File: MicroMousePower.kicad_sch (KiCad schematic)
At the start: 25 parts, among them J1 USB_C_Receptacle_PowerOnly_6P, J2 Conn_02x16_Odd_Even, T1 TIP31C, U1 INA219AxDCN, U2 MCP73831-3-MC, U3 CH224K, U4 DRV8833PW

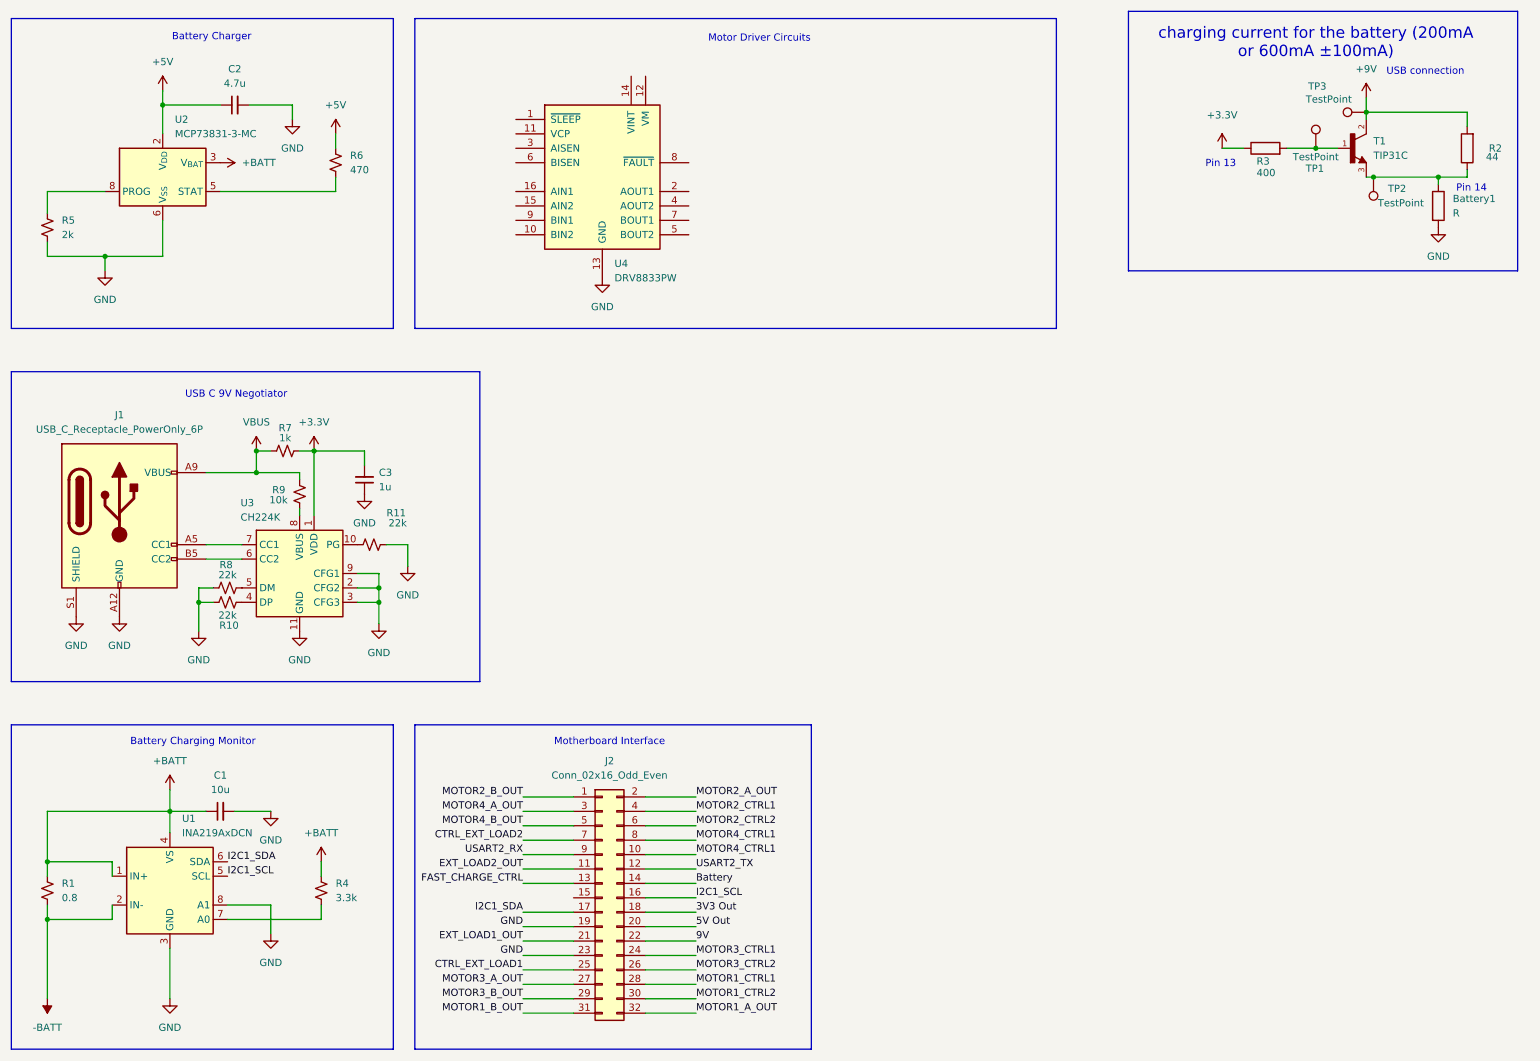
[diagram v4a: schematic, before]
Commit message: connected motor driver circuit
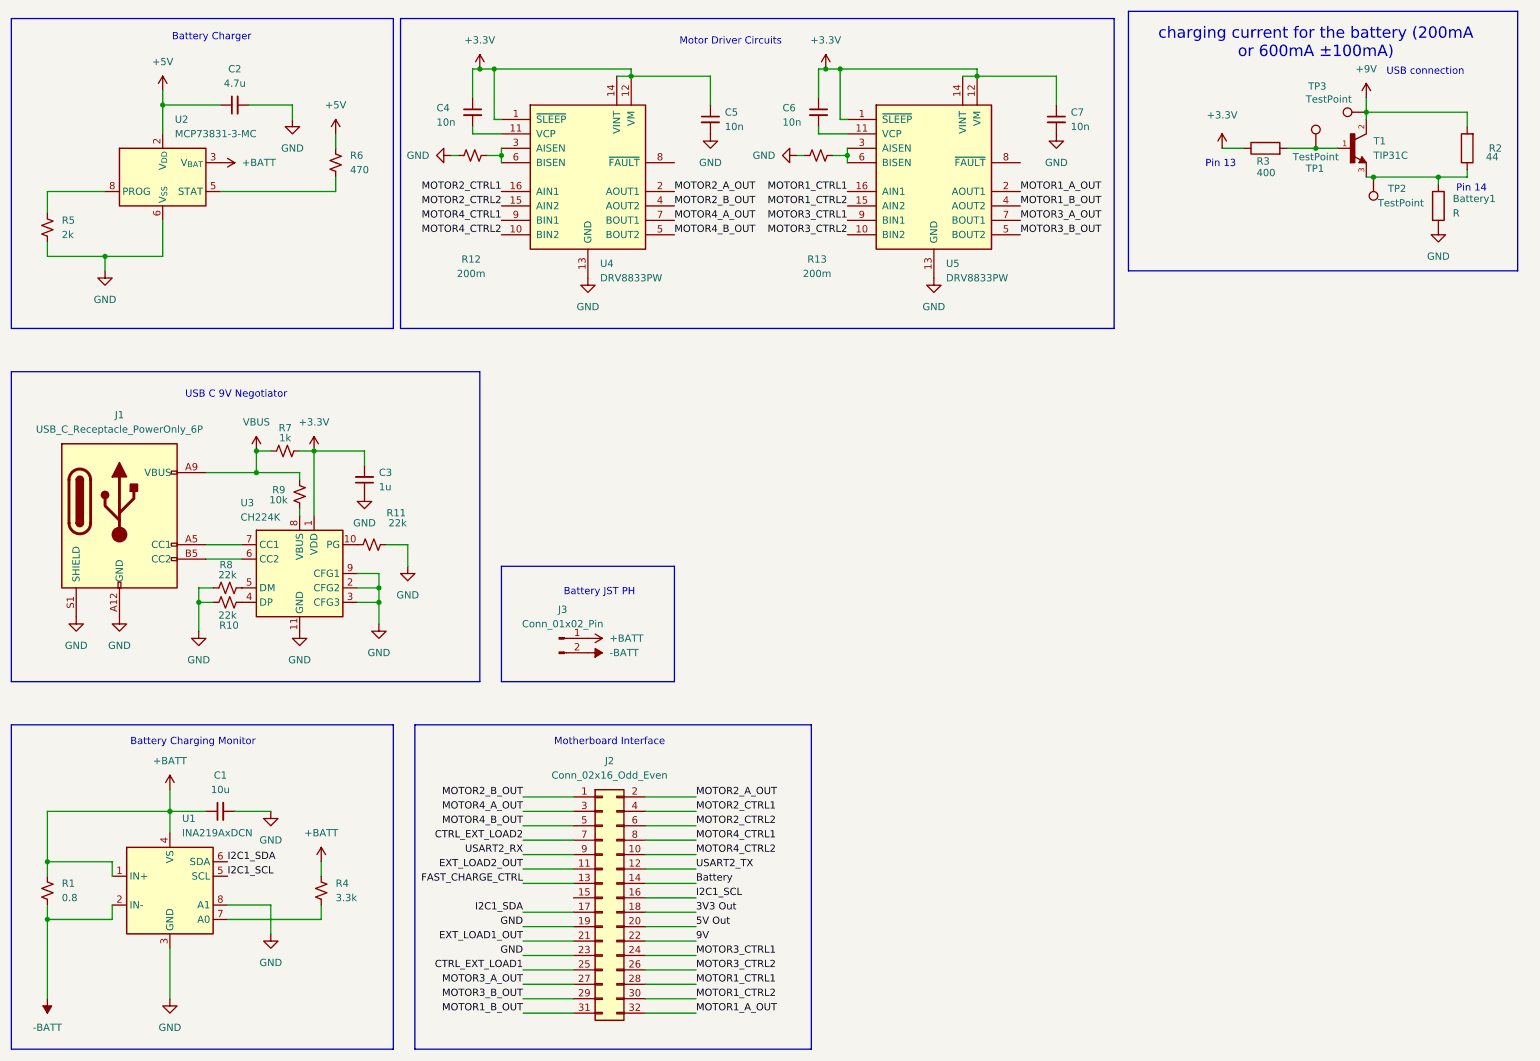
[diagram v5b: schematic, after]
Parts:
- added C4, C5, C6, C7: 10n, symbol Device:C_Small
- added J3: Conn_01x02_Pin, symbol Connector:Conn_01x02_Pin
- added R12, R13: 200m, symbol Device:R_Small_US
- added U5: DRV8833PW, Package_SO:TSSOP-16_4.4x5mm_P0.65mm, symbol Driver_Motor:DRV8833PW
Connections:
- net +3.3V: now also U4.1 (~{SLEEP}), U4.12 (VM), U4.14 (VINT), C4.1, C5.1, C6.1, C7.1, U5.1 (~{SLEEP}), U5.12 (VM), U5.14 (VINT)
- net +BATT: now also J3.1 (Pin_1)
- net -BATT: now also J3.2 (Pin_2)
- net GND: now also C5.2, C7.2, R12.1, R13.1, U5.13 (GND)
- net MOTOR1_A_OUT: now also U5.2 (AOUT1)
- net MOTOR1_B_OUT: now also U5.4 (AOUT2)
- net MOTOR1_CTRL1: now also U5.16 (AIN1)
- net MOTOR1_CTRL2: now also U5.15 (AIN2)
- net MOTOR2_A_OUT: now also U4.2 (AOUT1)
- net MOTOR2_B_OUT: now also U4.4 (AOUT2)
- net MOTOR2_CTRL1: now also U4.16 (AIN1)
- net MOTOR2_CTRL2: now also U4.15 (AIN2)
- net MOTOR3_A_OUT: now also U5.7 (BOUT1)
- net MOTOR3_B_OUT: now also U5.5 (BOUT2)
- net MOTOR3_CTRL1: now also U5.9 (BIN1)
- net MOTOR3_CTRL2: now also U5.10 (BIN2)
- net MOTOR4_A_OUT: now also U4.7 (BOUT1)
- net MOTOR4_B_OUT: now also U4.5 (BOUT2)
- net MOTOR4_CTRL1: now also U4.9 (BIN1); no longer J2.10 (Pin_10)
- net MOTOR4_CTRL2: now reaches U4.10 (BIN2)
- net MOTOR4_CTRL2: now also J2.10 (Pin_10)
- net at U4.11 (VCP): now also C4.2
- net at U4.3 (AISEN): now also U4.6 (BISEN), R12.2
- new net: C6.2, U5.11 (VCP)
- new net: R13.2, U5.3 (AISEN), U5.6 (BISEN)
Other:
- note added: "Battery JST PH"
- moved on the sheet: U4

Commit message: power flag defintions for ERC
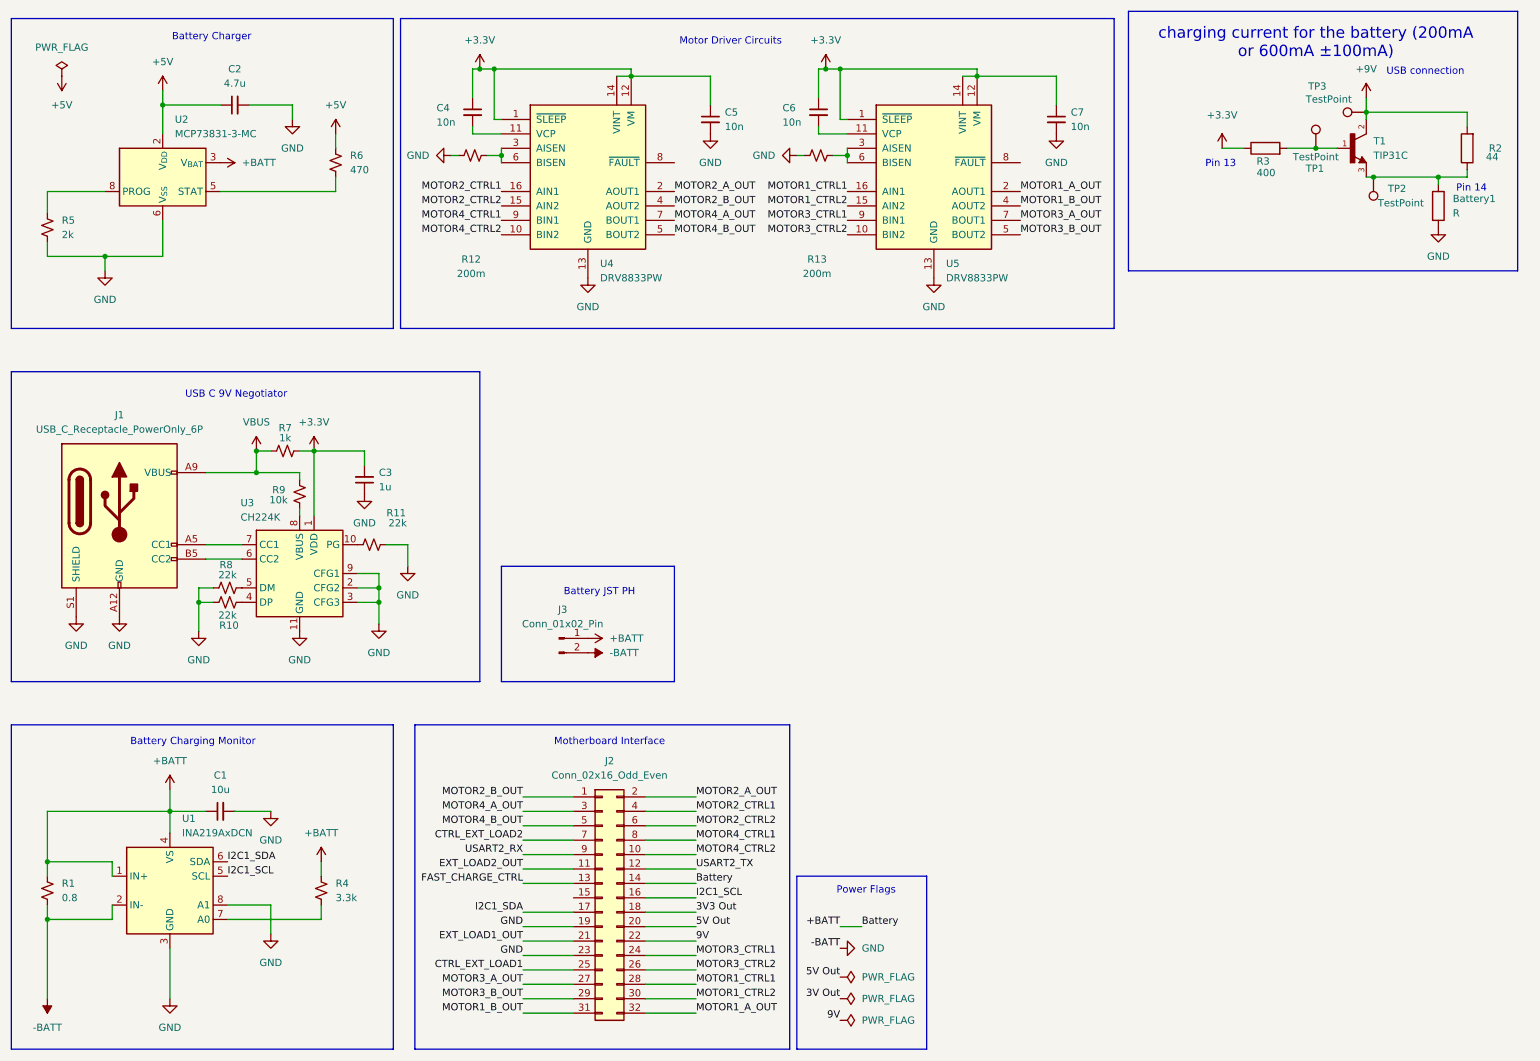
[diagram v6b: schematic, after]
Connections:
- net Battery is gone; now on net +BATT: J2.14 (Pin_14)
- net GND is gone; now on net -BATT: Battery1.2, C1.2, C2.2, C3.1, C5.2, C7.2, J1.A12 (GND), J1.B12 (GND), J1.S1 (SHIELD), J2.19 (Pin_19), J2.23 (Pin_23), R10.2, R11.2, R12.1, R13.1, R5.2, R8.1, U1.3 (GND), U1.8 (A1), U2.6 (V_{SS}), U3.11 (GND), U3.2 (CFG2), U3.3 (CFG3), U3.9 (CFG1), U4.13 (GND), U5.13 (GND)
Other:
- note added: "Power Flags"

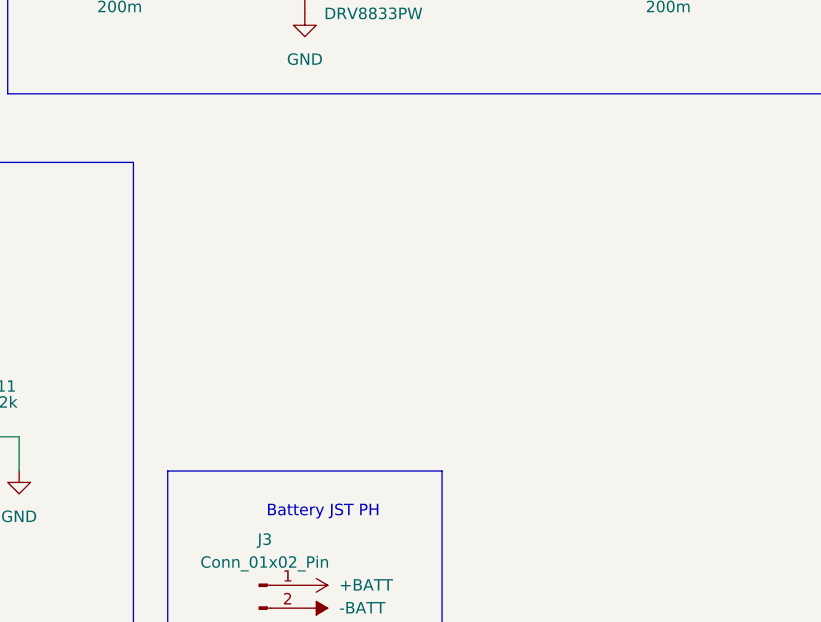
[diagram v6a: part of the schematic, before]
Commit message: template for step down IC
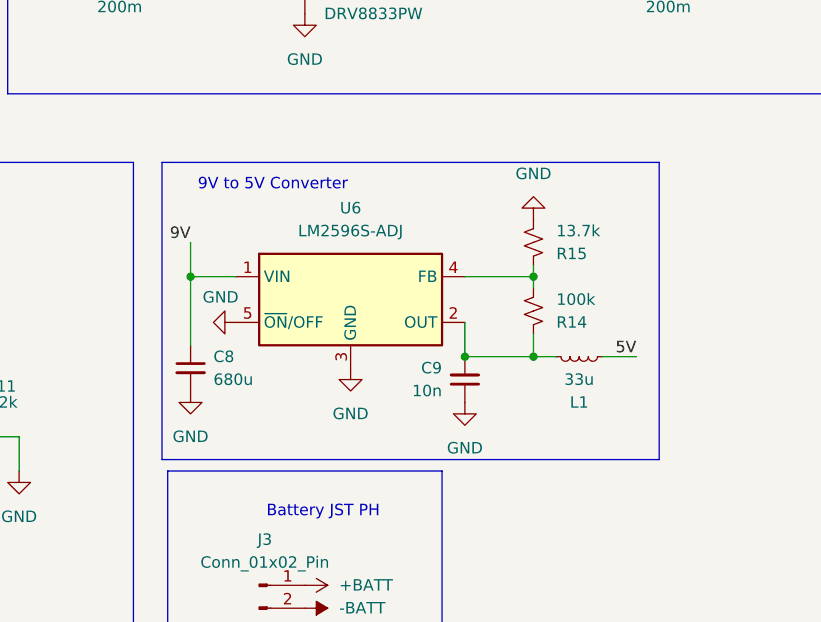
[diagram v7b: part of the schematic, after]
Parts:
- added C8: 680u, symbol Device:C_Small
- added C9: 10n, symbol Device:C_Small
- added L1: 33u, symbol Device:L_Small
- added R14: 100k, symbol Device:R_Small_US
- added R15: 13.7k, symbol Device:R_Small_US
- added U6: LM2596S-ADJ, Package_TO_SOT_SMD:TO-263-5_TabPin3, symbol Regulator_Switching:LM2596S-ADJ
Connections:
- net -BATT: now also C8.2, C9.1, R15.2, U6.3 (GND), U6.5 (~{ON}/OFF)
- net 9V: now also C8.1, U6.1 (VIN)
- new net: C9.2, L1.1, R14.1, U6.2 (OUT)
- new net: R14.2, R15.1, U6.4 (FB)
- new net 5V: L1.2
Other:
- note added: "9V to 5V Converter"

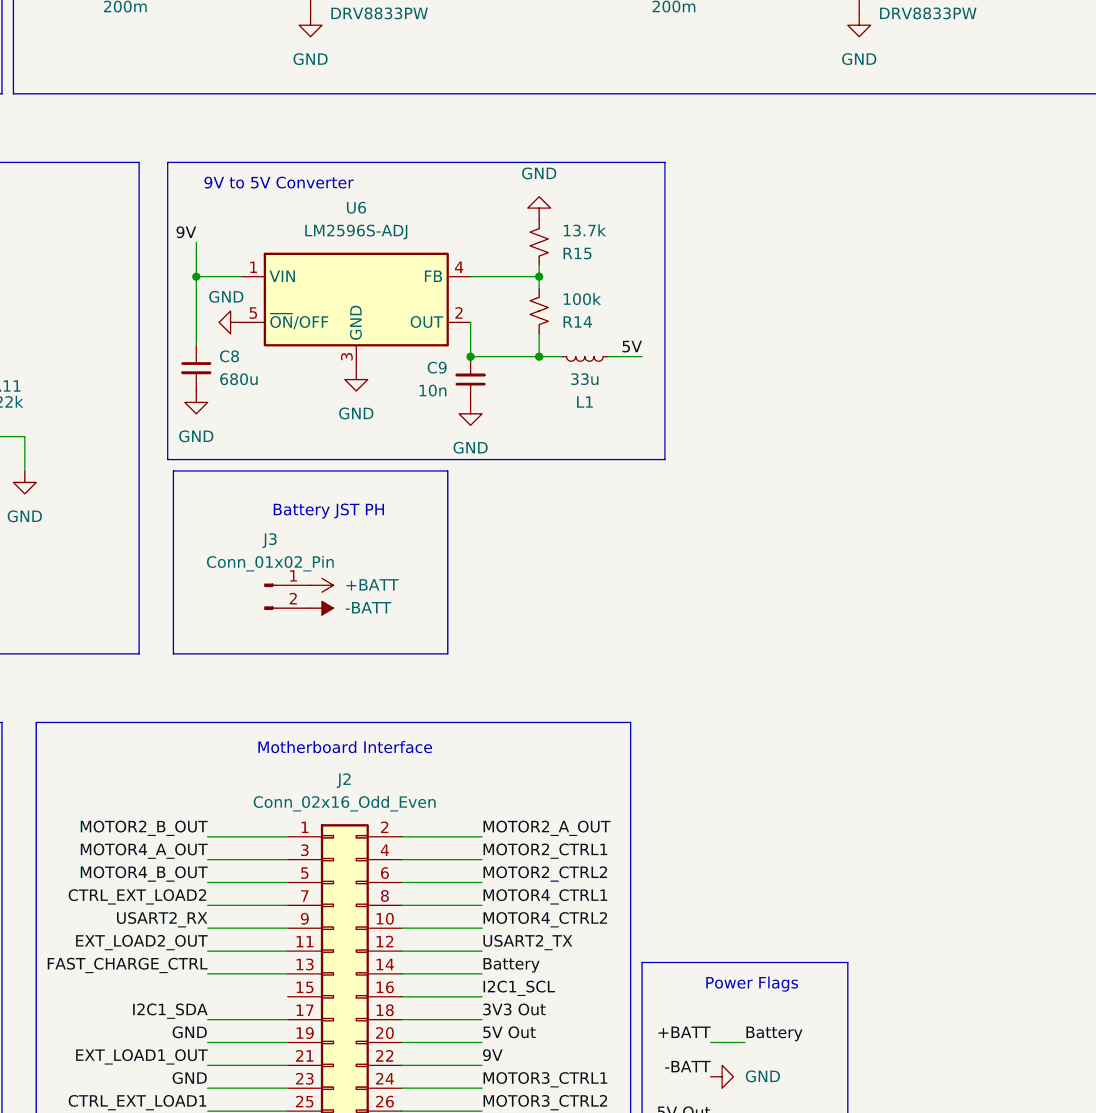
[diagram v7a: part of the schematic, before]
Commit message: added 3V6 to 3V3 step down
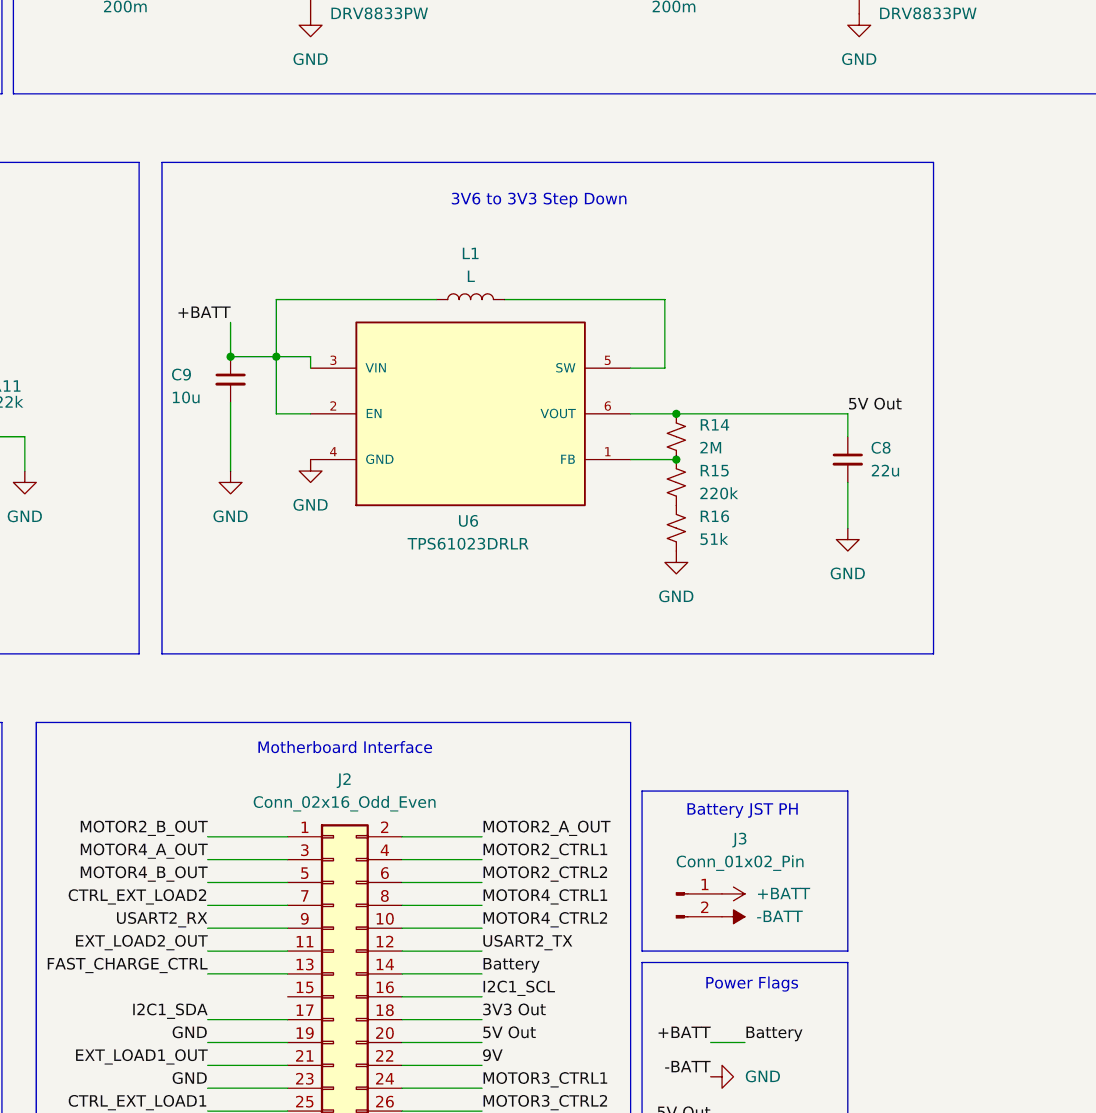
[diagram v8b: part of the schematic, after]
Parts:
- removed L1: 33u, symbol Device:L_Small
- removed U6: LM2596S-ADJ, Package_TO_SOT_SMD:TO-263-5_TabPin3, symbol Regulator_Switching:LM2596S-ADJ
- added L1: L, symbol Device:L
- added R16: 51k, symbol Device:R_Small_US
- added U6: TPS61023DRLR, TPS61023DRLR:DRL0006A, symbol TPS61023DRLR:TPS61023DRLR
- C8: value 680u -> 22u
- C9: value 10n -> 10u
- J1: footprint (none) -> Connector_USB:USB_C_Receptacle_GCT_USB4125-xx-x_6P_TopMnt_Horizontal
- J2: footprint (none) -> Connector_PinHeader_2.54mm:PinHeader_2x16_P2.54mm_Horizontal
- R14: value 100k -> 2M
- R15: value 13.7k -> 220k
- TP1: footprint (none) -> TestPoint:TestPoint_2Pads_Pitch2.54mm_Drill0.8mm
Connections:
- net +BATT: now also C9.1, L1.1, U6.2 (EN), U6.3 (VIN)
- net -BATT: now also C9.2, R16.2, U6.4 (GND); no longer C9.1, R15.2
- net 5V Out: now also C8.1, R14.1, U6.6 (VOUT)
- net 9V: no longer C8.1
- net at R14.2, R15.1: now also U6.1 (FB)
- new net: L1.2, U6.5 (SW)
- new net: R15.2, R16.1
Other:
- note added: "3V6 to 3V3 Step Down"
- note removed: "9V to 5V Converter"
- moved on the sheet: J3
